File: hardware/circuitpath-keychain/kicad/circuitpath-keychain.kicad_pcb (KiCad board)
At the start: 2 copper layers, 118 x 24 mm, 115 parts, among them J1 USB-A plug (PCB fingers), J2 USB-C (vertical), J3 ISP pads, SW1 Button, SW2 Button, U1 ATmega32U4-AU, U2 MAX7219CWG+T, U3 MAX7219CWG+T, U4 USBLC6-2SC6, Y1 16MHz

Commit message: Keychain: fix stacked USB-A finger pads, space decoupling caps, add 2D renders
The pad-overlap check now catches stacked pads (the USB-A fingers were all at one point).

Co-Authored-By: Claude Sonnet 5.5 <noreply@anthropic.com>
Claude-Session: https://claude.ai/code/session_01DPLfCi4mjQi9VLJYecUoR3
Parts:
- moved C6 2.20 mm to (49.8, -8.40)
- moved C7 1.40 mm to (53.0, -8.40)
- moved C5 1.00 mm to (61.0, -8.40)
- moved C8 0.61 mm to (57.0, -8.90)

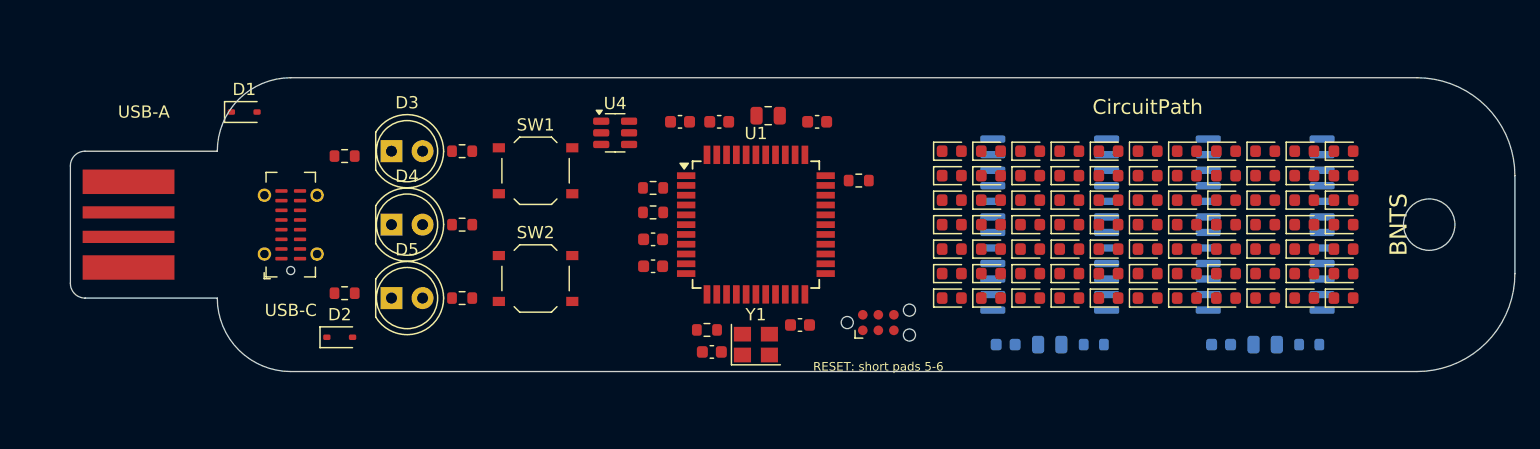
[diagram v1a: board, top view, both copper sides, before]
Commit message: Keychain: clear logo/text zone before keyring hole, add piezo buzzer, compact layout
Co-Authored-By: Claude Sonnet 5.5 <noreply@anthropic.com>
Claude-Session: https://claude.ai/code/session_01DPLfCi4mjQi9VLJYecUoR3
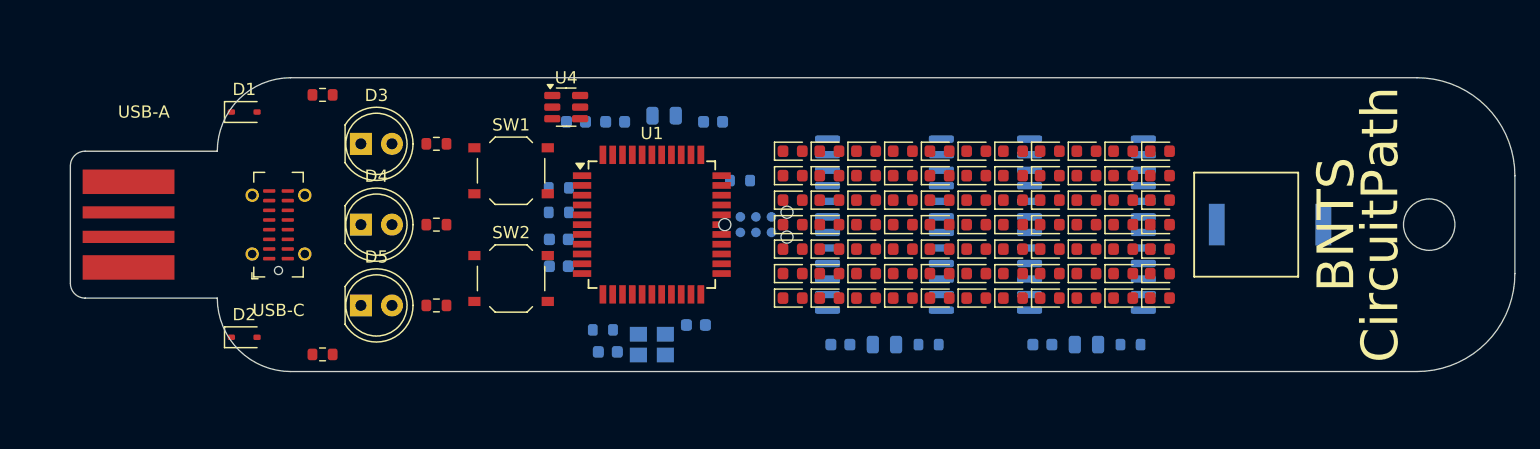
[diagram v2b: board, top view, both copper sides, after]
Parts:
- added BZ1: Piezo 9x9, Buzzer_Murata_PKMCS0909E, B.Cu at (98.0, 0.00)
- C1, C2, C3, C4, C5, C6, C7, C8, J3, R3, R4, R5, R6, Y1: moved to B.Cu
- moved D76 15.0 mm to (89.0, -6.00)
- moved D77 15.0 mm to (89.0, -4.00)
- moved D78 15.0 mm to (89.0, -2.00)
- moved D79 15.0 mm to (89.0, 0.00)
- moved D80 15.0 mm to (89.0, 2.00)
- moved D81 15.0 mm to (89.0, 4.00)
- moved D82 15.0 mm to (89.0, 6.00)
- moved D69 14.8 mm to (86.0, -6.00)
- moved D70 14.8 mm to (86.0, -4.00)
- moved D71 14.8 mm to (86.0, -2.00)
- moved D72 14.8 mm to (86.0, 0.00)
- moved D73 14.8 mm to (86.0, 2.00)
- moved D74 14.8 mm to (86.0, 4.00)
- moved D75 14.8 mm to (86.0, 6.00)
- moved C11 14.6 mm to (79.4, 9.80)
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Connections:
- U1 pad 29: (no net) -> BUZZ_A
- U1 pad 30: (no net) -> BUZZ_B
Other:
- board text added: "Banyule Nillumbik"
- board text added: "RESET = short pads 5+6"
- board text added: "Tech School"
- board text removed: "Banyule Nillumbik Tech School"
- board text removed: "RESET: short pads 5-6"

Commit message: Keychain: BNTS logo from SVG on silkscreen, KiCad-model 3D renders, buzzer on back
Co-Authored-By: Claude Sonnet 5.5 <noreply@anthropic.com>
Claude-Session: https://claude.ai/code/session_01DPLfCi4mjQi9VLJYecUoR3
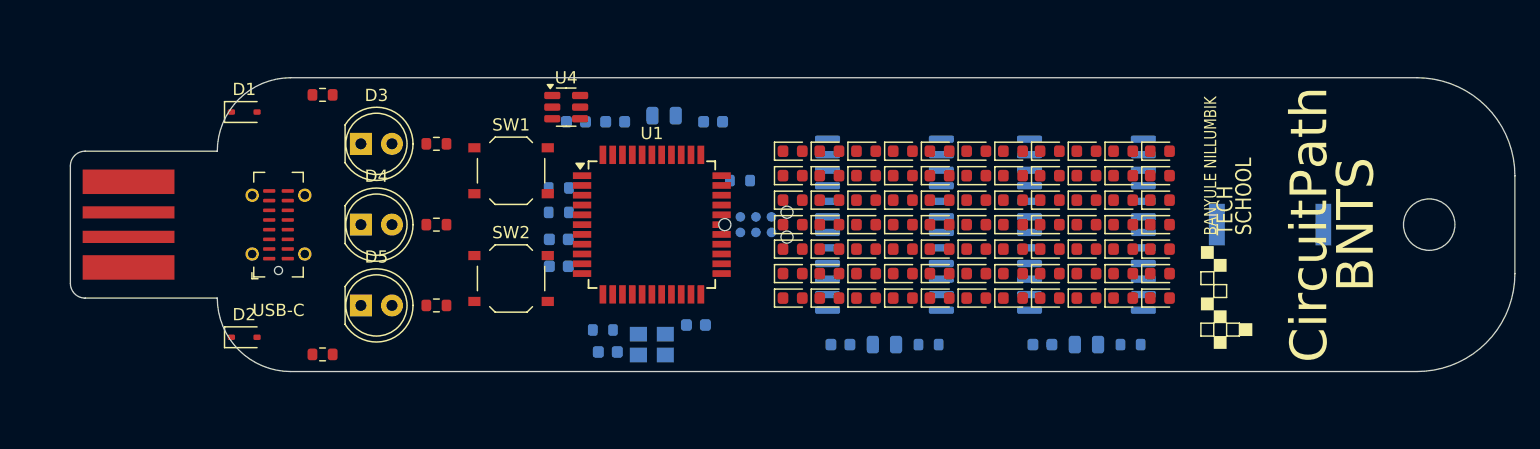
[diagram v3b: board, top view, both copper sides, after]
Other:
- board text added: "BANYULE NILLUMBIK"
- board text added: "SCHOOL"
- board text added: "TECH"
- board text removed: "USB-A"

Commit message: Keychain: route board with Freerouting, export Gerbers + drill, DRC-clean at JLCPCB-style limits
Layout fixes found by KiCad DRC: ISP pads without alignment holes, diodes off the corner,
LED row pitch 2.4 mm, CC resistors on back, hand-tied USB-C data pins, edge keep-out band.

Co-Authored-By: Claude Sonnet 5.5 <noreply@anthropic.com>
Claude-Session: https://claude.ai/code/session_01DPLfCi4mjQi9VLJYecUoR3
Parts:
- J3: footprint Tag-Connect_TC2030-IDC-NL_2x03_P1.27mm_Vertical -> CircuitPath:ISP_Pads_2x3
- R1, R2: moved to B.Cu
- moved R1 14.0 mm to (13.0, 1.20)
- moved R2 11.8 mm to (20.9, -1.17)
- moved D1 2.31 mm to (16.5, -9.40)
- moved D2 2.31 mm to (16.5, 9.40)
- moved D13 1.20 mm to (62.0, -7.20)
- moved D20 1.20 mm to (65.0, -7.20)
- moved D27 1.20 mm to (68.0, -7.20)
- moved D34 1.20 mm to (71.0, -7.20)
- moved D41 1.20 mm to (74.0, -7.20)
- moved D48 1.20 mm to (77.0, -7.20)
- moved D55 1.20 mm to (80.0, -7.20)
- moved D6 1.20 mm to (59.0, -7.20)
- moved D62 1.20 mm to (83.0, -7.20)
- moved D69 1.20 mm to (86.0, -7.20)
- moved D76 1.20 mm to (89.0, -7.20)
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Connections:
- J2 pad A9: VBUS_C -> (no net)
- J2 pad B4: VBUS_C -> (no net)
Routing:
- net USB_DM: track 0.00 -> 4.12 mm, vias 0 -> 2
- net USB_DP: track 0.00 -> 2.18 mm, vias 0 -> 1
